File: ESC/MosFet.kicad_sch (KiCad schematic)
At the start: 34 parts, among them J2 Conn_01x03, Q1 BSC028N06LS3, Q2 BSC028N06LS3, U2 IRS2101

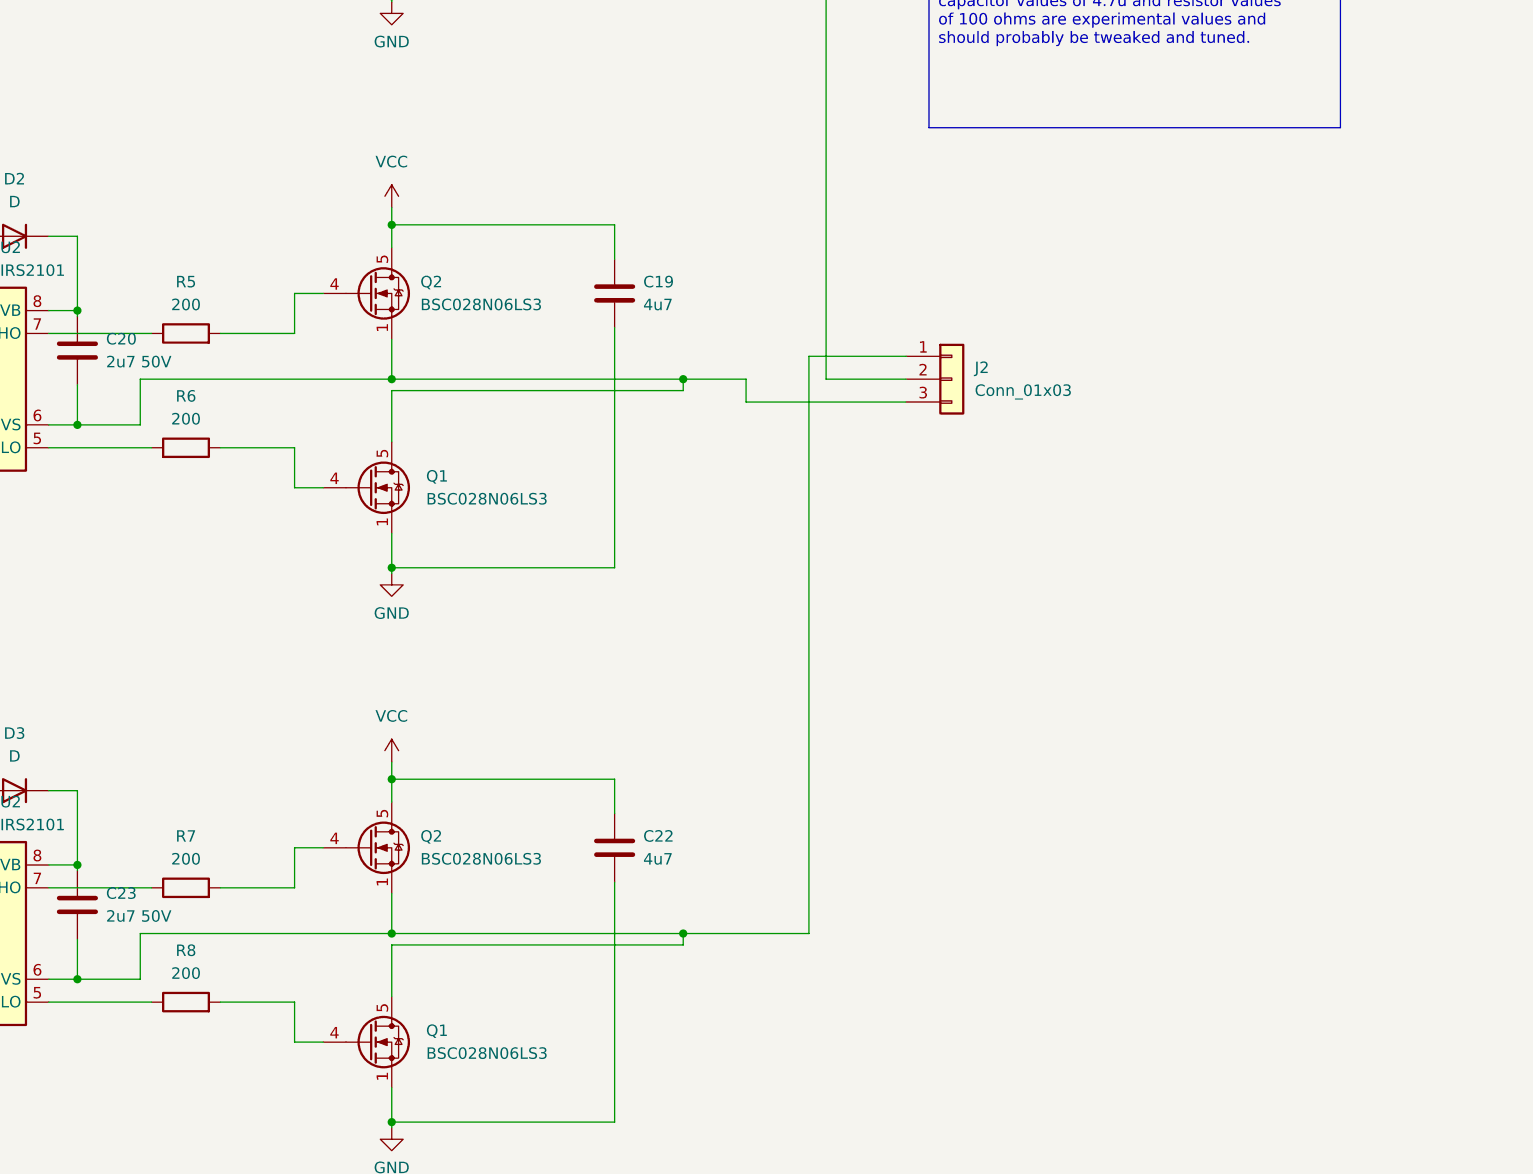
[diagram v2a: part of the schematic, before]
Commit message: did some of the routing ofthe PCB
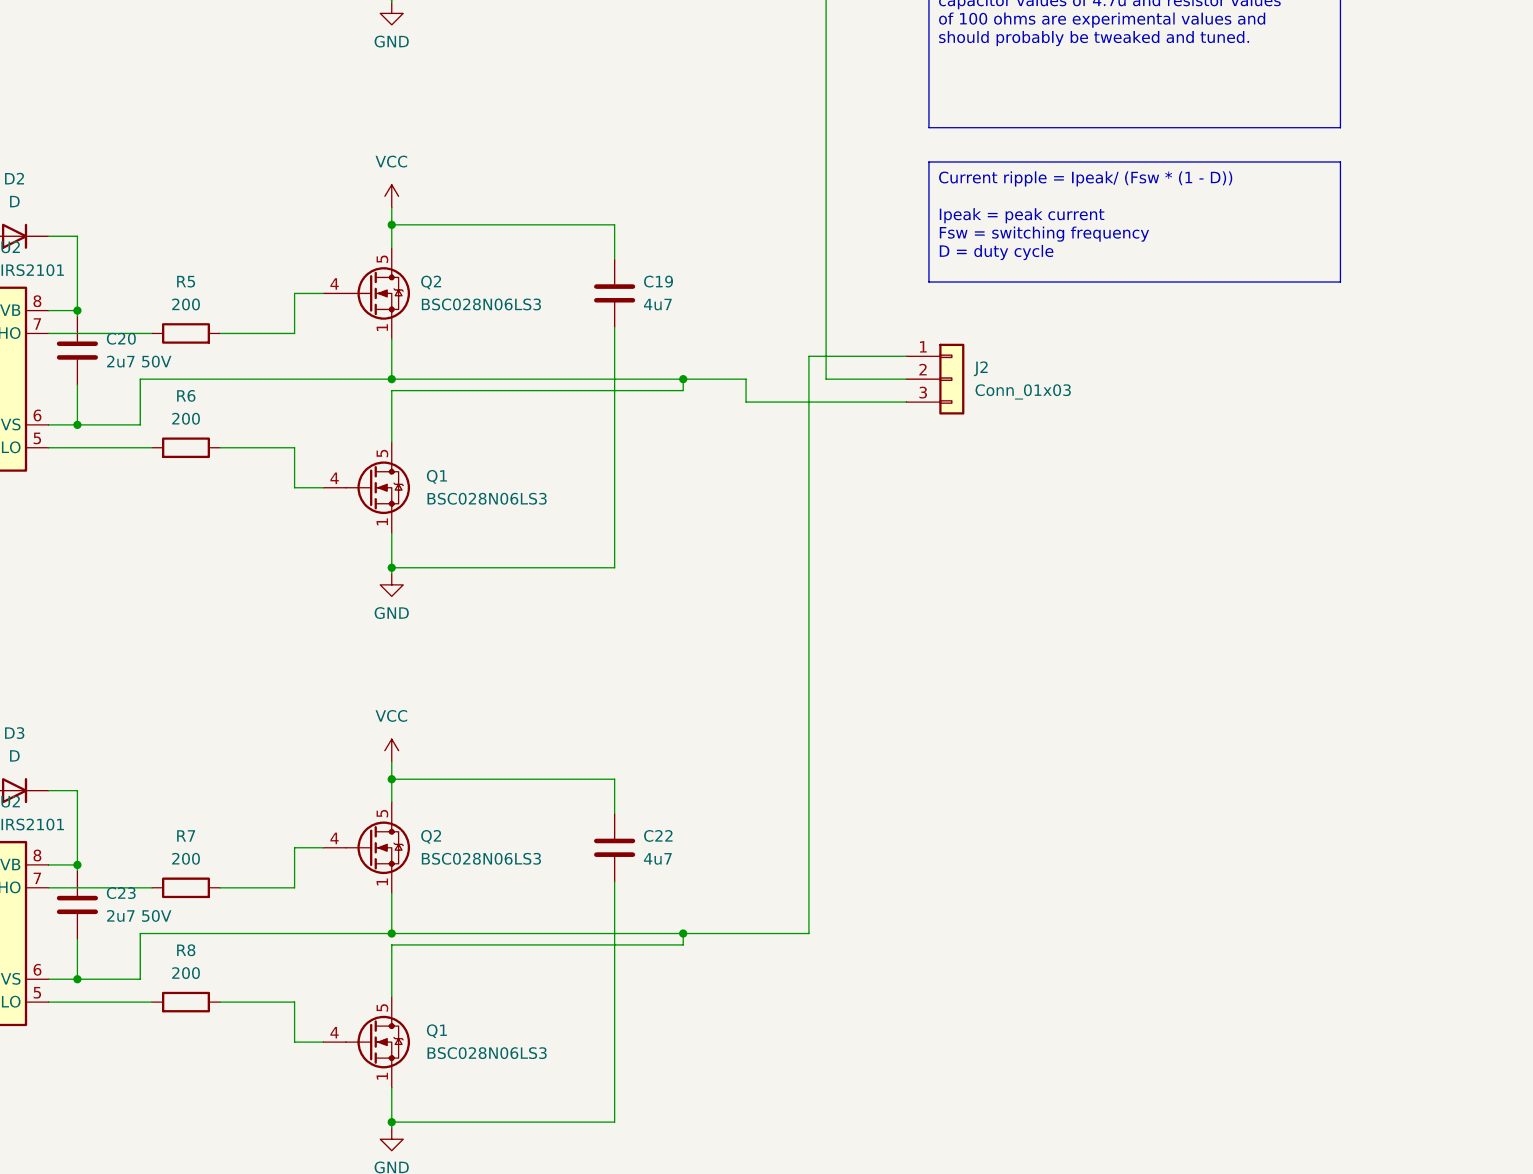
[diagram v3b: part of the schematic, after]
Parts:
- J2: footprint TerminalBlock_Phoenix:TerminalBlock_Phoenix_MKDS-1,5-3_1x03_P5.00mm_Horizontal -> Connector_AMASS:AMASS_MR30PW-FB_1x03_P3.50mm_Horizontal
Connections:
- net at R8.1: now also Q1.4 (G); no longer U2.5 (LO)
- net at R8.2: now also U2.5 (LO); no longer Q1.4 (G)
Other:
- moved on the sheet: R8
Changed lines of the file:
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@@
+    (effects (font (size 1.27 1.27)) (justify left top))
+  )
+  (text_box "Current ripple = Ipeak/ (Fsw * (1 - D))\n\nIpeak = peak current\nFsw = switching frequency\nD = duty cycle"
+    (at 184.15 88.265 0) (size 45.72 13.335)
+    (stroke (width 0) (type default))
+    (fill (type none))
     (effects (font (size 1.27 1.27)) (justify left top))
   )
@@
     )
   )
-  (symbol (lib_id "Device:R") (at 101.6 181.61 90) (unit 1)
-    (in_bom yes) (on_board yes) (dnp no) (fields_autoplaced)
+  (symbol (lib_id "Device:R") (at 101.6 181.61 270) (mirror x) (unit 1)
+    (in_bom yes) (on_board yes) (dnp no)
     (property "Reference" "R8" (at 101.6 175.895 90)
       (effects (font (size 1.27 1.27)))
@@
       (effects (font (size 1.27 1.27)) (justify left))
     )
-    (property "Footprint" "TerminalBlock_Phoenix:TerminalBlock_Phoenix_MKDS-1,5-3_1x03_P5.00mm_Horizontal" (at 186.69 112.395 0)
-      (effects (font (size 1.27 1.27)) hide)
-    )
+    (property "Footprint" "Connector_AMASS:AMASS_MR30PW-FB_1x03_P3.50mm_Horizontal" (at 186.69 112.395 0)
+      (effects (font (size 1.27 1.27)) hide)
+    )

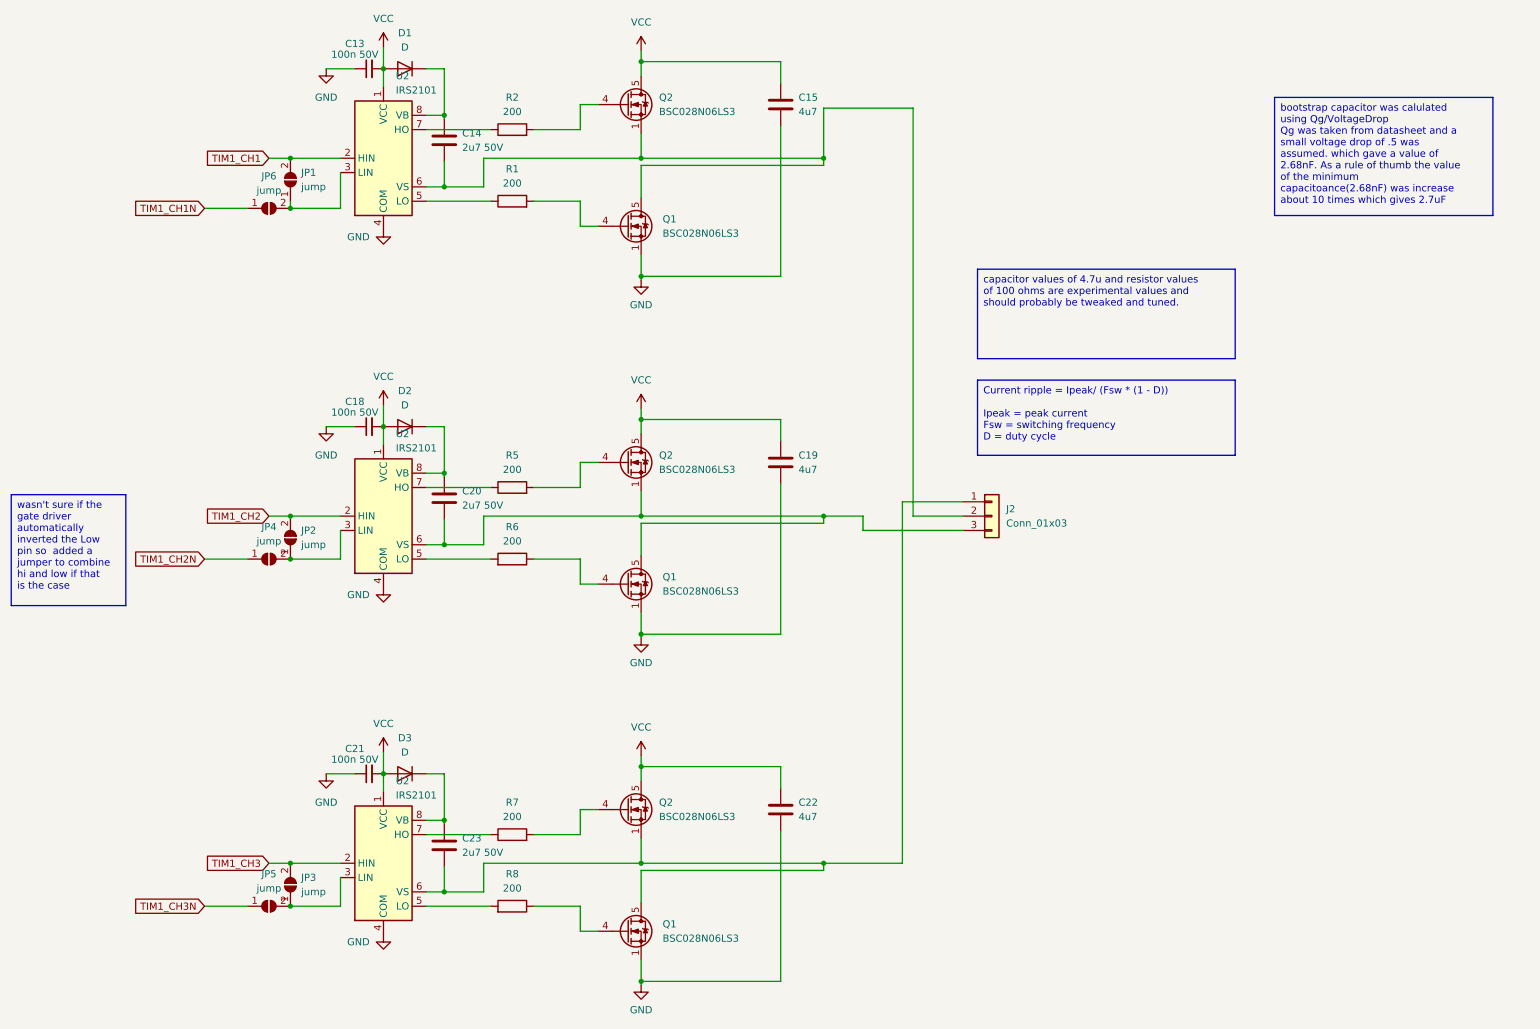
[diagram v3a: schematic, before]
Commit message: finished the pcb layout of the ESC and now need to be revised to make sure everything is correct
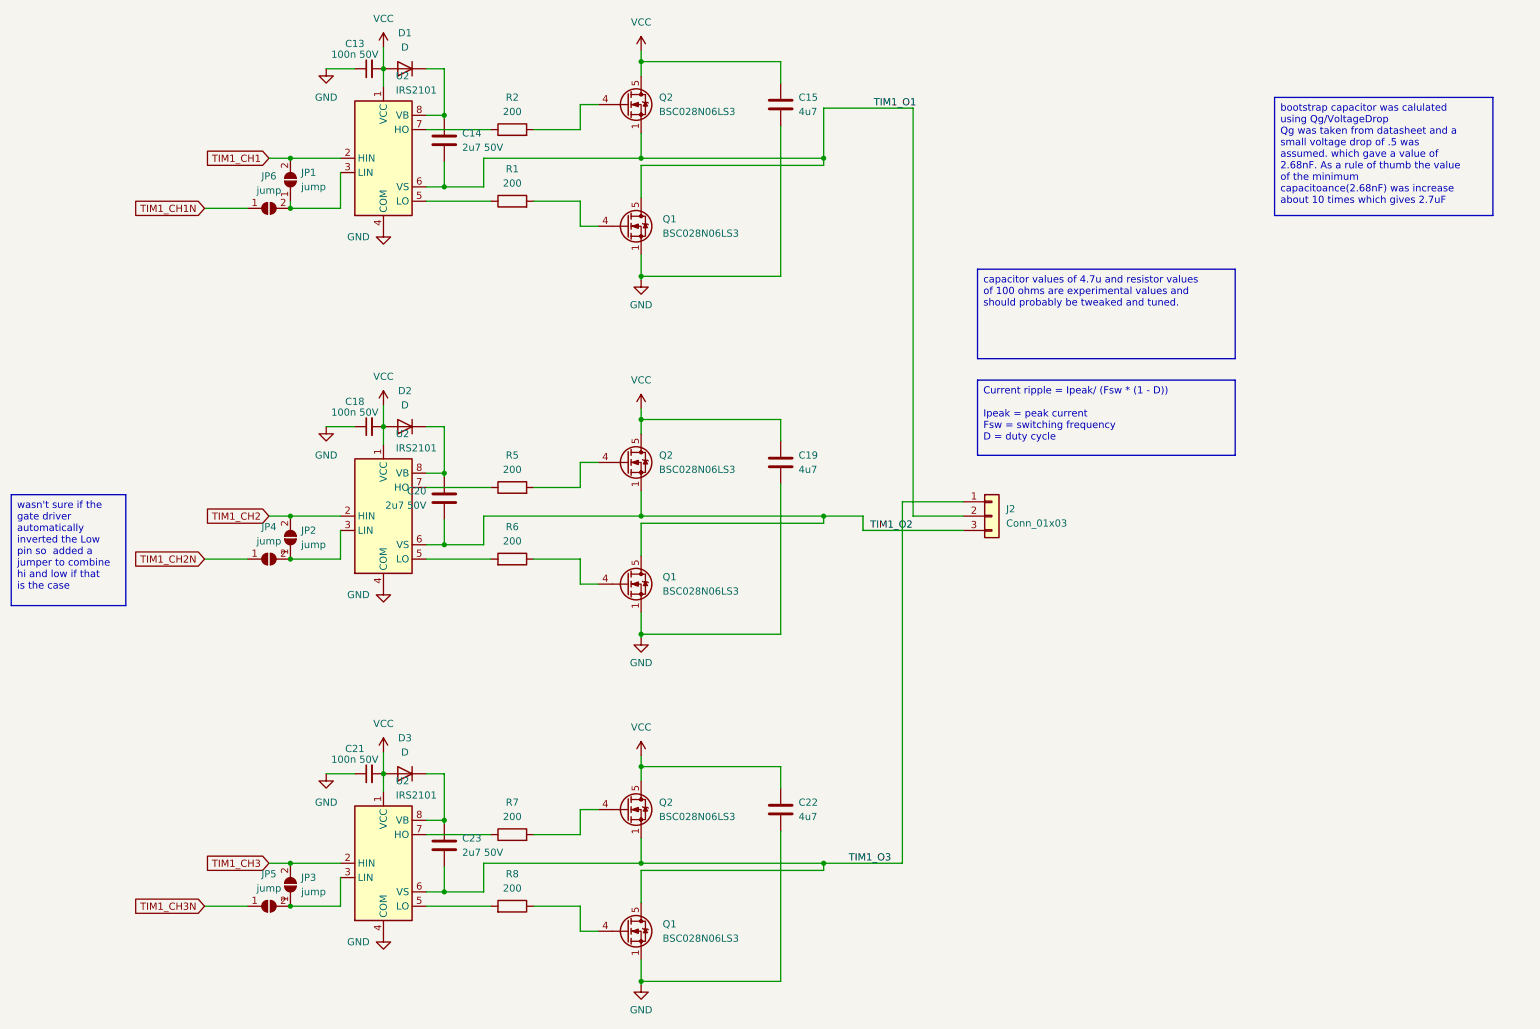
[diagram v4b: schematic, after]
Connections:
- net TIM1_O1: now reaches C14.2, J2.2 (Pin_2), Q1.5 (D), Q2.1 (S), Q2.2 (S), Q2.3 (S), U2.6 (VS)
- net TIM1_O2: now reaches C20.2, J2.3 (Pin_3), Q1.5 (D), Q2.1 (S), Q2.2 (S), Q2.3 (S), U2.6 (VS)
- net TIM1_O3: now reaches C23.2, J2.1 (Pin_1), Q1.5 (D), Q2.1 (S), Q2.2 (S), Q2.3 (S), U2.6 (VS)
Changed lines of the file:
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@@
     (effects (font (size 1.27 1.27)) (justify left top))
+  )
+  (label "TIM1_O2" (at 165.1 114.935 0) (fields_autoplaced)
+    (effects (font (size 1.27 1.27)) (justify left bottom))
+  )
+  (label "TIM1_O1" (at 165.735 40.005 0) (fields_autoplaced)
+    (effects (font (size 1.27 1.27)) (justify left bottom))
+  )
+  (label "TIM1_O3" (at 161.29 173.99 0) (fields_autoplaced)
+    (effects (font (size 1.27 1.27)) (justify left bottom))
   )
   (global_label "TIM1_CH3N" (shape input) (at 46.99 181.61 180) (fields_autoplaced)
@@
     )
   )
-  (symbol (lib_id "Device:C") (at 89.535 109.22 0) (unit 1)
-    (in_bom yes) (on_board yes) (dnp no) (fields_autoplaced)
-    (property "Reference" "C20" (at 92.71 107.95 0)
-      (effects (font (size 1.27 1.27)) (justify left))
-    )
-    (property "Value" "2u7 50V " (at 92.71 110.49 0)
-      (effects (font (size 1.27 1.27)) (justify left))
-    )
-    (property "Footprint" "Capacitor_SMD:C_0603_1608Metric_Pad1.08x0.95mm_HandSolder" (at 90.5002 113.03 0)
+  (symbol (lib_id "Device:C") (at 89.535 109.22 0) (mirror y) (unit 1)
+    (in_bom yes) (on_board yes) (dnp no)
+    (property "Reference" "C20" (at 86.36 107.95 0)
+      (effects (font (size 1.27 1.27)) (justify left))
+    )
+    (property "Value" "2u7 50V " (at 86.36 110.49 0)
+      (effects (font (size 1.27 1.27)) (justify left))
+    )
+    (property "Footprint" "Capacitor_SMD:C_0603_1608Metric_Pad1.08x0.95mm_HandSolder" (at 88.5698 113.03 0)
       (effects (font (size 1.27 1.27)) hide)
     )
@@
   )
   (symbol (lib_id "Connector_Generic:Conn_01x03") (at 186.69 112.395 0) (unit 1)
-    (in_bom yes) (on_board yes) (dnp no) (fields_autoplaced)
+    (in_bom yes) (on_board yes) (dnp no)
     (property "Reference" "J2" (at 189.23 111.125 0)
       (effects (font (size 1.27 1.27)) (justify left))
